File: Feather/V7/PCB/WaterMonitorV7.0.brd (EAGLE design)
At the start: 100 x 46 mm, 45 parts, among them IC1 BME680, J3 Flow1, J4 Flow2, J6 Temperature2, J7 Temperature1, Q1 4.3A/20V/54mΩ, Q3 220mA/50V/3.5Ω

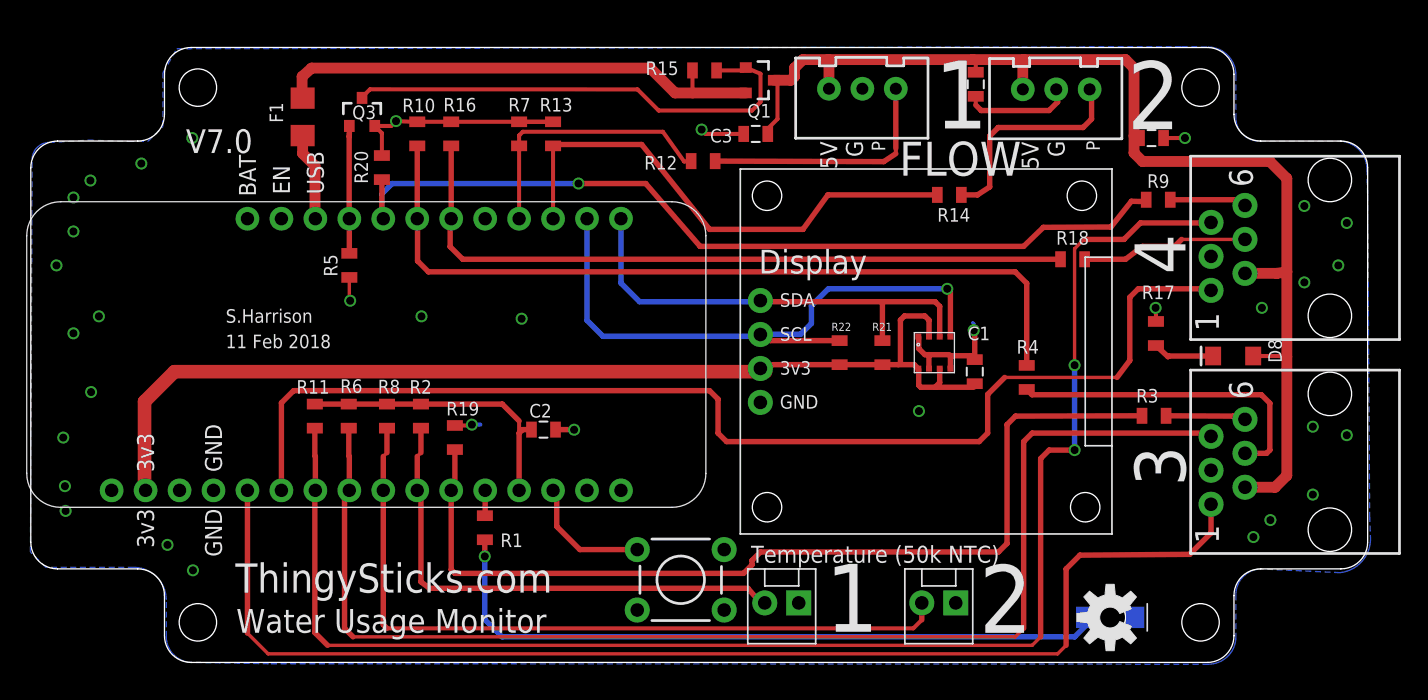
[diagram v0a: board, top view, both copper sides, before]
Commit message: Moved OSH LED, added values.
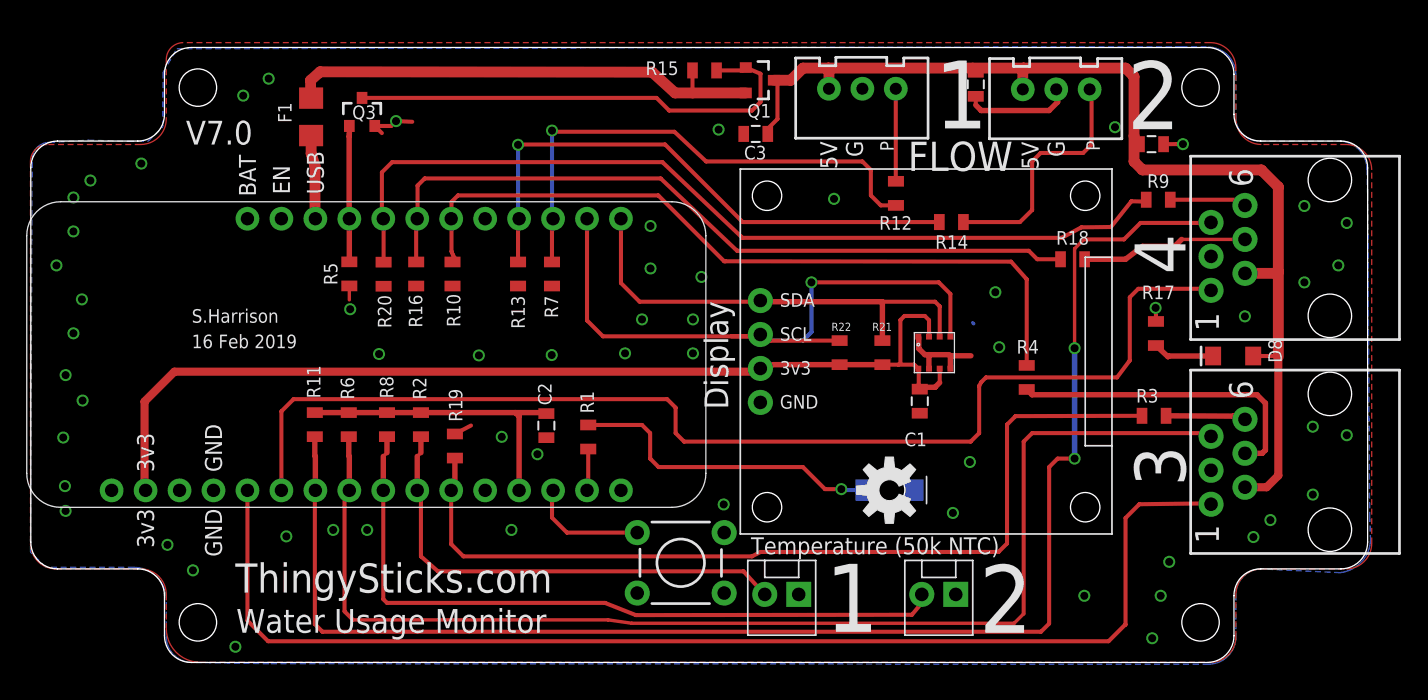
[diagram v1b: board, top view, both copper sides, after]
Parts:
- Q1: value 4.3A/20V/54mΩ -> IRLML2244TRPBF
- Q3: value 220mA/50V/3.5Ω -> BSS138PW
- moved D1 19.1 mm to (64.3, 12.9)
- moved LOGO1 19.1 mm to (64.3, 12.9)
- moved R12 14.6 mm to (64.7, 35.1), turned to 90 degrees
- moved R10 10.8 mm to (31.6, 29.0), turned to 270 degrees
- moved R13 10.8 mm to (36.5, 29.0), turned to 270 degrees
- moved R16 10.8 mm to (28.9, 29.0), turned to 270 degrees
- moved R7 10.8 mm to (39.0, 29.0), turned to 270 degrees
- moved R1 10.3 mm to (41.7, 16.9), turned to 90 degrees
- moved R20 7.98 mm to (26.4, 29.0), turned to 270 degrees
- moved C1 4.67 mm to (66.5, 19.5), turned to 90 degrees
- moved R14 2.04 mm to (68.9, 32.9)
- moved S1 1.27 mm to (48.6, 7.44)
- moved F1 0.64 mm to (21.0, 40.8)
- moved R19 0.64 mm to (31.8, 16.2)
- moved R5 0.64 mm to (23.9, 29.1)
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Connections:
- net FLOW_1: now also MS1.19; no longer MS1.20
- net FLOW_2: now also MS1.20; no longer MS1.19
- net FLOW_3: now also MS1.22; no longer MS1.23
- net FLOW_4: now also MS1.23; no longer MS1.22
- net OSH_LOGO_LED: now also MS1.15; no longer MS1.12
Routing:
- net N$21: track 52.4 -> 23.9 mm
- net GND: track 48.2 -> 24.0 mm, vias 35 -> 59
- net FLOW_1: track 20.4 -> 39.0 mm, vias 0 -> 1
- net N$1: track 18.5 -> 6.93 mm
- net FLOW_SENSOR_POWER: track 88.5 -> 83.2 mm
- net SCL: track 47.8 -> 52.2 mm
- net FLOW_3: track 61.0 -> 56.9 mm
- net 3.3V: track 80.8 -> 77.0 mm
- net FLOW_2: track 39.4 -> 42.7 mm, vias 0 -> 1
- net LED_1: track 71.2 -> 68.1 mm
- net TEMPERATURE_3: track 94.8 -> 91.8 mm
- net FLOW_4: track 53.6 -> 56.5 mm
- net TEMPERATURE_2: track 56.7 -> 53.9 mm
- net TEMPERATURE_4: track 112.5 -> 110.1 mm
- net TEMPERATURE_1: track 38.1 -> 36.1 mm
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- added copper zone on layer 1, net GND
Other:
- board text added: "16 Feb 2019"
- board text removed: "11 Feb 2018"
